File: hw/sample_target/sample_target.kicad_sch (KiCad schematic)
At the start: 27 parts, among them J1 USB_C_Receptacle, SW1 BTN, SW2 BTN, U1 SN74AHC1G08DBVRG4, U2 MIC5504-3.3YM5, U3 TMUX1511PWR, U4 STM32L412C8T6

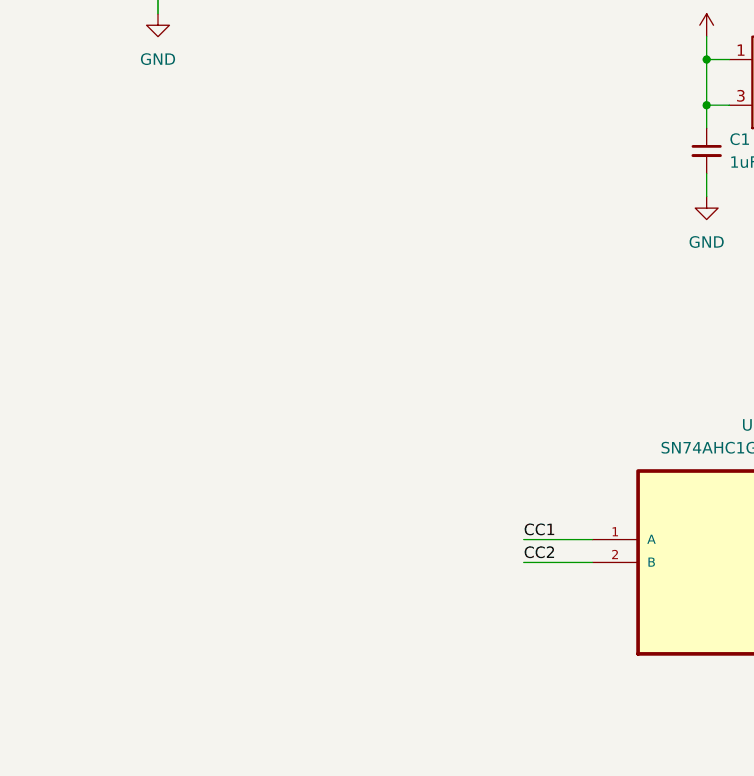
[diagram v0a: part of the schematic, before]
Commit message: Added opamp to sample target
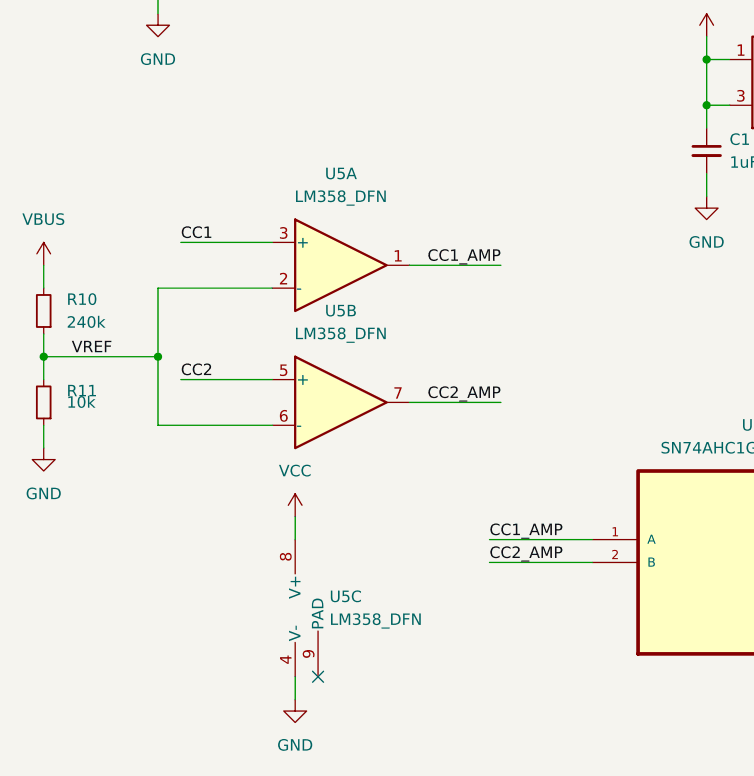
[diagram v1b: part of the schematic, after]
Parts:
- added R10: 240k, Resistor_SMD:R_0402_1005Metric, symbol Device:R_Small
- added R11: 10k, Resistor_SMD:R_0402_1005Metric, symbol Device:R_Small
- added U5: LM358_DFN, Package_DFN_QFN:DFN-8-1EP_2x2mm_P0.5mm_EP1.05x1.75mm, symbol Amplifier_Operational:LM358_DFN
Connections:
- net CC1: now also U5.3 (+); no longer U1.1 (A)
- net CC2: now also U5.5 (+); no longer U1.2 (B)
- net GND: now also R11.1, U5.4 (V-)
- net VBUS: now also R10.2
- net VCC: now also U5.8 (V+)
- new net CC1_AMP: U1.1 (A), U5.1
- new net CC2_AMP: U1.2 (B), U5.7
- new net VREF: R10.1, R11.2, U5.2 (-), U5.6 (-)
- no-connect marks 33 -> 34

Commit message: Added sample target part numbers
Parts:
- J1: MPN (none) -> USB4056-03-A
- SW1, SW2: MPN (none) -> PTS820J25MSMTRLFS
- U1: MPN (none) -> SN74AHC1G08DBVRG4
- U2: MPN (none) -> MIC5504-3.3YM5-TR
- U3: MPN (none) -> TMUX1511PWR
- U4: MPN (none) -> STM32L412C8T6
- U5: MPN (none) -> LM358QT
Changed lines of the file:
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@@
       (effects (font (size 1.27 1.27)) (justify left bottom) hide)
+    )
+    (property "MPN" "TMUX1511PWR" (id 4) (at 127 53.34 0)
+      (effects (font (size 1.27 1.27)) hide)
     )
     (pin "1")
@@
       (effects (font (size 1.27 1.27)) hide)
     )
+    (property "MPN" "LM358QT" (id 4) (at 53.34 152.4 0)
+      (effects (font (size 1.27 1.27)) hide)
+    )
     (pin "5")
     (pin "6")
@@
     )
     (property "Datasheet" "www.st.com/resource/en/datasheet/lm358.pdf" (id 3) (at 50.8 175.26 0)
+      (effects (font (size 1.27 1.27)) hide)
+    )
+    (property "MPN" "LM358QT" (id 4) (at 50.8 175.26 0)
       (effects (font (size 1.27 1.27)) hide)
     )
@@
       (effects (font (size 1.27 1.27)) hide)
     )
+    (property "MPN" "LM358QT" (id 4) (at 53.34 137.16 0)
+      (effects (font (size 1.27 1.27)) hide)
+    )
     (pin "1")
     (pin "2")
@@
       (effects (font (size 1.27 1.27)) hide)
     )
+    (property "MPN" "PTS820J25MSMTRLFS" (id 4) (at 256.54 66.04 0)
+      (effects (font (size 1.27 1.27)) hide)
+    )
     (pin "1")
     (pin "2")
@@
     )
     (property "Datasheet" "http://ww1.microchip.com/downloads/en/DeviceDoc/MIC550X.pdf" (id 3) (at 100.33 110.49 0)
+      (effects (font (size 1.27 1.27)) hide)
+    )
+    (property "MPN" "MIC5504-3.3YM5-TR" (id 4) (at 106.68 116.84 0)
       (effects (font (size 1.27 1.27)) hide)
     )
@@
     )
     (property "Datasheet" "https://www.usb.org/sites/default/files/documents/usb_type-c.zip" (id 3) (at 36.83 66.04 0)
+      (effects (font (size 1.27 1.27)) hide)
+    )
+    (property "MPN" "USB4056-03-A" (id 4) (at 33.02 66.04 0)
       (effects (font (size 1.27 1.27)) hide)
     )
@@
       (effects (font (size 1.524 1.524)))
     )
+    (property "MPN" "STM32L412C8T6" (id 4) (at 198.12 144.78 0)
+      (effects (font (size 1.27 1.27)) hide)
+    )
     (pin "1")
     (pin "23")
@@
     (property "Datasheet" "" (id 3) (at 149.86 27.94 0)
       (effects (font (size 1.524 1.524)))
+    )
+    (property "MPN" "STM32L412C8T6" (id 4) (at 213.36 76.2 0)
+      (effects (font (size 1.27 1.27)) hide)
     )
     (pin "10")
@@
       (effects (font (size 1.27 1.27)) hide)
     )
+    (property "MPN" "PTS820J25MSMTRLFS" (id 4) (at 264.16 43.18 0)
+      (effects (font (size 1.27 1.27)) hide)
+    )
     (pin "1")
     (pin "2")
@@
       (effects (font (size 1.27 1.27)) (justify left bottom) hide)
     )
-    (pin "1")
+    (property "MPN" "SN74AHC1G08DBVRG4" (id 4) (at 99.06 170.18 0)
+      (effects (font (size 1.27 1.27)) hide)
+    )
+    (pin "1")
